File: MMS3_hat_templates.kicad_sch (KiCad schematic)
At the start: 10 parts

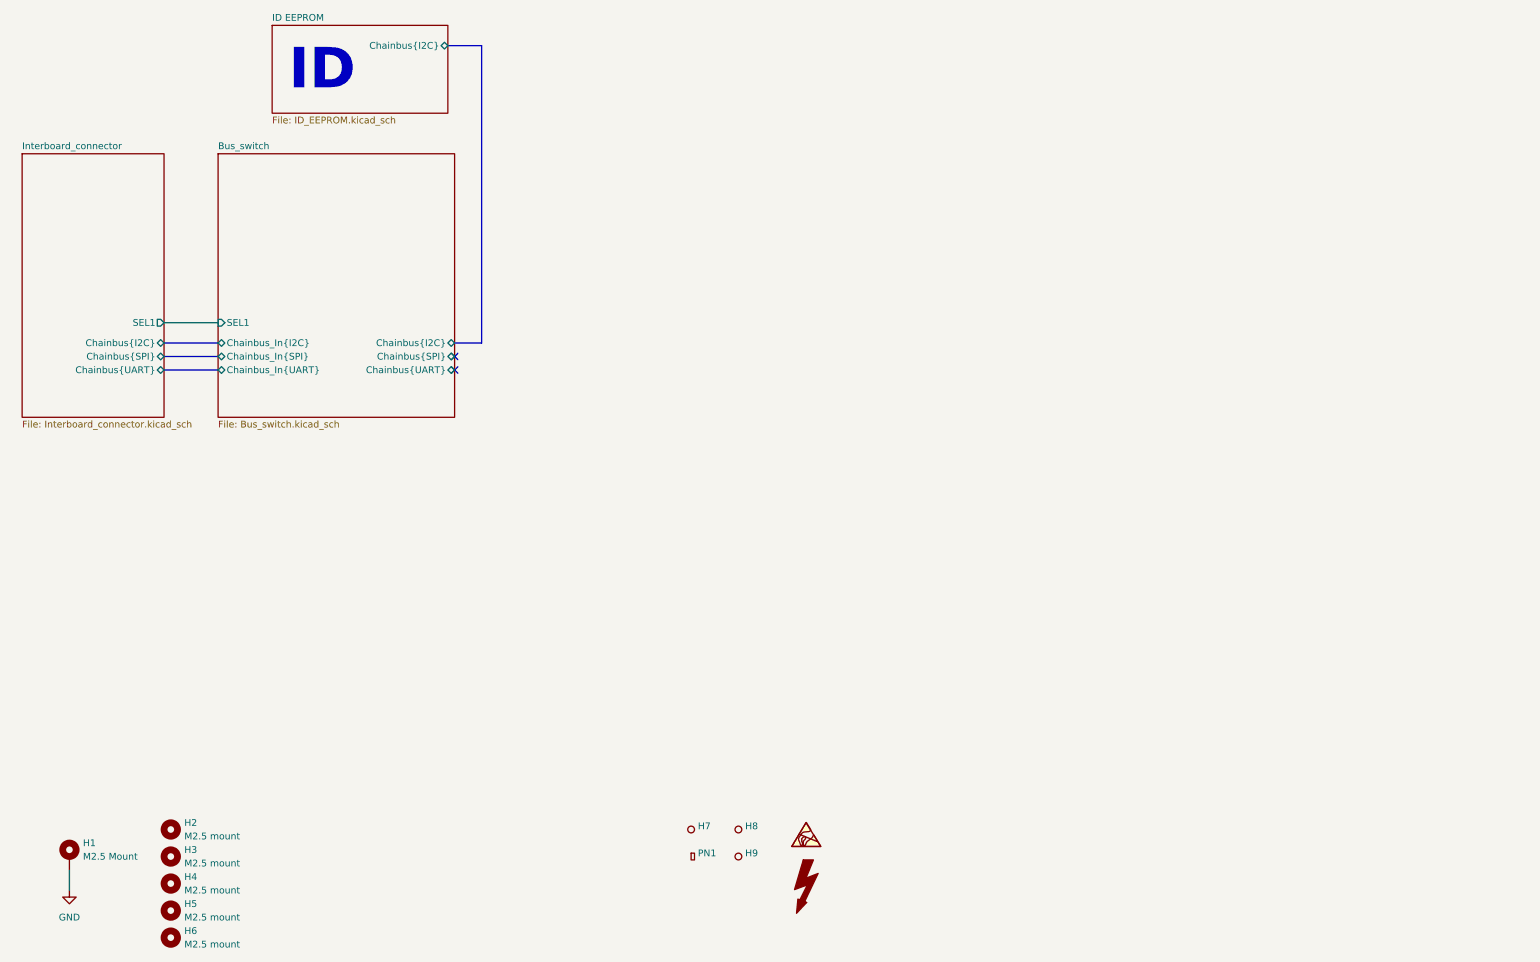
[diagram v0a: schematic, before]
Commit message: first steps
 thermocouple and GPIO expander sheets done
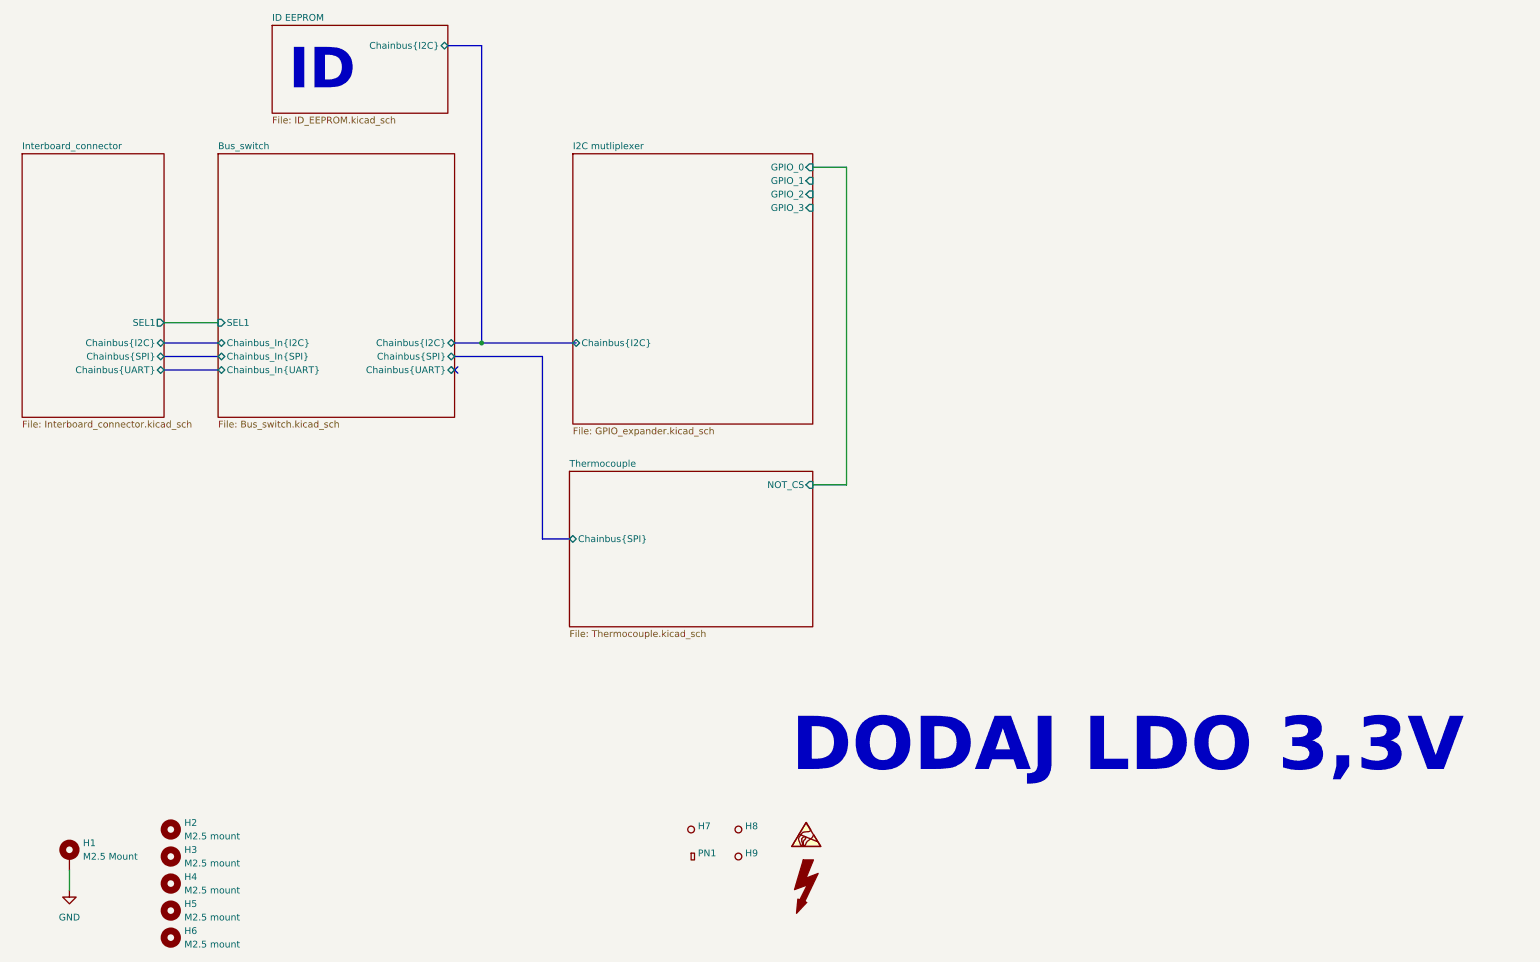
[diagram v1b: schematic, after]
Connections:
- no-connect marks 2 -> 1
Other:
- added sheet I2C mutliplexer (GPIO_expander.kicad_sch)
- added sheet Thermocouple (Thermocouple.kicad_sch)
- note added: "DODAJ LDO 3,3V"
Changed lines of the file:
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@@
 		)
 	)
-	(no_connect
-		(at 96.52 82.55)
+	(text "DODAJ LDO 3,3V "
+		(exclude_from_sim no)
+		(at 223.012 153.162 0)
+		(effects
+			(font
+				(size 10 10)
+				(thickness 4.4)
+				(bold yes)
+			)
+		)
+	)
+	(junction
+		(at 101.6 77.47)
+		(diameter 0)
+		(color 0 0 0 0)
 	)
 	(no_connect
-		(at 96.52 80.01)
+		(at 96.52 82.55)
 	)
 	(bus
@@
 		)
 	)
+	(bus
+		(pts
+			(xy 101.6 77.47) (xy 119.38 77.47)
+		)
+		(stroke
+			(width 0)
+			(type default)
+		)
+	)
 	(wire
 		(pts
@@
 		)
 	)
+	(wire
+		(pts
+			(xy 170.18 104.14) (xy 170.18 44.45)
+		)
+		(stroke
+			(width 0)
+			(type default)
+		)
+	)
 	(bus
 		(pts
@@
 		)
 	)
+	(bus
+		(pts
+			(xy 96.52 80.01) (xy 113.03 80.01)
+		)
+		(stroke
+			(width 0)
+			(type default)
+		)
+	)
+	(bus
+		(pts
+			(xy 113.03 80.01) (xy 113.03 114.3)
+		)
+		(stroke
+			(width 0)
+			(type default)
+		)
+	)
+	(wire
+		(pts
+			(xy 170.18 44.45) (xy 163.83 44.45)
+		)
+		(stroke
+			(width 0)
+			(type default)
+		)
+	)
+	(bus
+		(pts
+			(xy 113.03 114.3) (xy 118.11 114.3)
+		)
+		(stroke
+			(width 0)
+			(type default)
+		)
+	)
+	(wire
+		(pts
+			(xy 163.83 104.14) (xy 170.18 104.14)
+		)
+		(stroke
+			(width 0)
+			(type default)
+		)
+	)
 	(image
 		(at 74.93 59.69)
@@
 				)
 			)
+		)
+	)
+	(sheet
+		(at 118.745 41.91)
+		(size 45.085 50.8)
+		(exclude_from_sim no)
+		(in_bom yes)
+		(on_board yes)
+		(dnp no)
+		(fields_autoplaced yes)
+		(stroke
+			(width 0.1524)
+			(type solid)
+		)
+		(fill
+			(color 0 0 0 0.0000)
+		)
+		(property "Sheetname" "I2C mutliplexer"
+			(at 118.745 41.1984 0)
+			(effects
+				(font
+					(size 1.27 1.27)
+				)
+				(justify left bottom)
+			)
+		)
+		(property "Sheetfile" "GPIO_expander.kicad_sch"
+			(at 118.745 93.2946 0)
+			(effects
+				(font
+					(size 1.27 1.27)
+				)
+				(justify left top)
+			)
+		)
+		(pin "Chainbus{I2C}" bidirectional
+			(at 118.745 77.47 180)
+			(effects
+				(font
+					(size 1.27 1.27)
+				)
+				(justify left)
+			)
+		)
+		(pin "GPIO_0" input
+			(at 163.83 44.45 0)
+			(effects
+				(font
+					(size 1.27 1.27)
+				)
+				(justify right)
+			)
+		)
+		(pin "GPIO_1" input
+			(at 163.83 46.99 0)
+			(effects
+				(font
+					(size 1.27 1.27)
+				)
+				(justify right)
+			)
+		)
+		(pin "GPIO_2" input
+			(at 163.83 49.53 0)
+			(effects
+				(font
+					(size 1.27 1.27)
+				)
+				(justify right)
+			)
+		)
+		(pin "GPIO_3" input
+			(at 163.83 52.07 0)
+			(effects
+				(font
+					(size 1.27 1.27)
+				)
+				(justify right)
+			)
+		)
+		(instances
+			(project "MMS3_hat_templates"
+				(path "/6596548a-44e0-46d8-8624-fd71cf4a3e17"
+					(page "5")
+				)
+			)
+		)
+	)
+	(sheet
+		(at 118.11 101.6)
+		(size 45.72 29.21)
+		(exclude_from_sim no)
+		(in_bom yes)
+		(on_board yes)
+		(dnp no)
+		(fields_autoplaced yes)
+		(stroke
+			(width 0.1524)
+			(type solid)
+		)
+		(fill
+			(color 0 0 0 0.0000)
+		)
+		(property "Sheetname" "Thermocouple"
+			(at 118.11 100.8884 0)
+			(effects
+				(font
+					(size 1.27 1.27)
+				)
+				(justify left bottom)
+			)
+		)
+		(property "Sheetfile" "Thermocouple.kicad_sch"
+			(at 118.11 131.3946 0)
+			(effects
+				(font
+					(size 1.27 1.27)
+				)
+				(justify left top)
+			)
+		)
+		(pin "Chainbus{SPI}" bidirectional
+			(at 118.11 114.3 180)
+			(effects
+				(font
+					(size 1.27 1.27)
+				)
+				(justify left)
+			)
+		)
+		(pin "NOT_CS" input
+			(at 163.83 104.14 0)
+			(effects
+				(font
+					(size 1.27 1.27)
+				)
+				(justify right)
+			)
+		)
+		(instances
+			(project "MMS3_hat_templates"
+				(path "/6596548a-44e0-46d8-8624-fd71cf4a3e17"
+					(page "6")
+				)
+			)

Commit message: done ( v 1.0 - check required )
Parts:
- removed H7, H8, H9: ~, PCM_JLCPCB:Hole_Tooling_JLCPCB, symbol PCM_JLCPCB-Manufacturing:Tooling Hole, PCM_JLCPCB, 1.152mm
- added C13, C14, C15: 10u, Capacitor_SMD:CP_Elec_3x5.4, symbol Device:C_Polarized
- added U14: AZ1117H-3.3TRE1, Package_TO_SOT_SMD:SOT-223-3_TabPin2, symbol Regulator_Linear:AZ1117H-ADJ
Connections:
- net GND: now also C13.2, C14.2, C15.2, U14.1 (GND)
- new net +3V3: C14.1, C15.1, U14.2 (VO)
- new net +5V: C13.1, U14.3 (VI)
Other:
- added sheet Thermocouple1 (Thermocouple.kicad_sch)
- added sheet Thermocouple2 (Thermocouple.kicad_sch)
- added sheet Thermocouple3 (Thermocouple.kicad_sch)
- added sheet Thermocouple4 (Thermocouple.kicad_sch)
- added sheet Thermocouple5 (Thermocouple.kicad_sch)
- added sheet Thermocouple6 (Thermocouple.kicad_sch)
- added sheet Thermocouple7 (Thermocouple.kicad_sch)
- added sheet Thermocouple8 (Thermocouple.kicad_sch)
- sheet I2C mutliplexer ports: added GPIO_4, GPIO_5, GPIO_6, GPIO_7, GPIO_8; removed none
- note removed: "DODAJ LDO 3,3V"

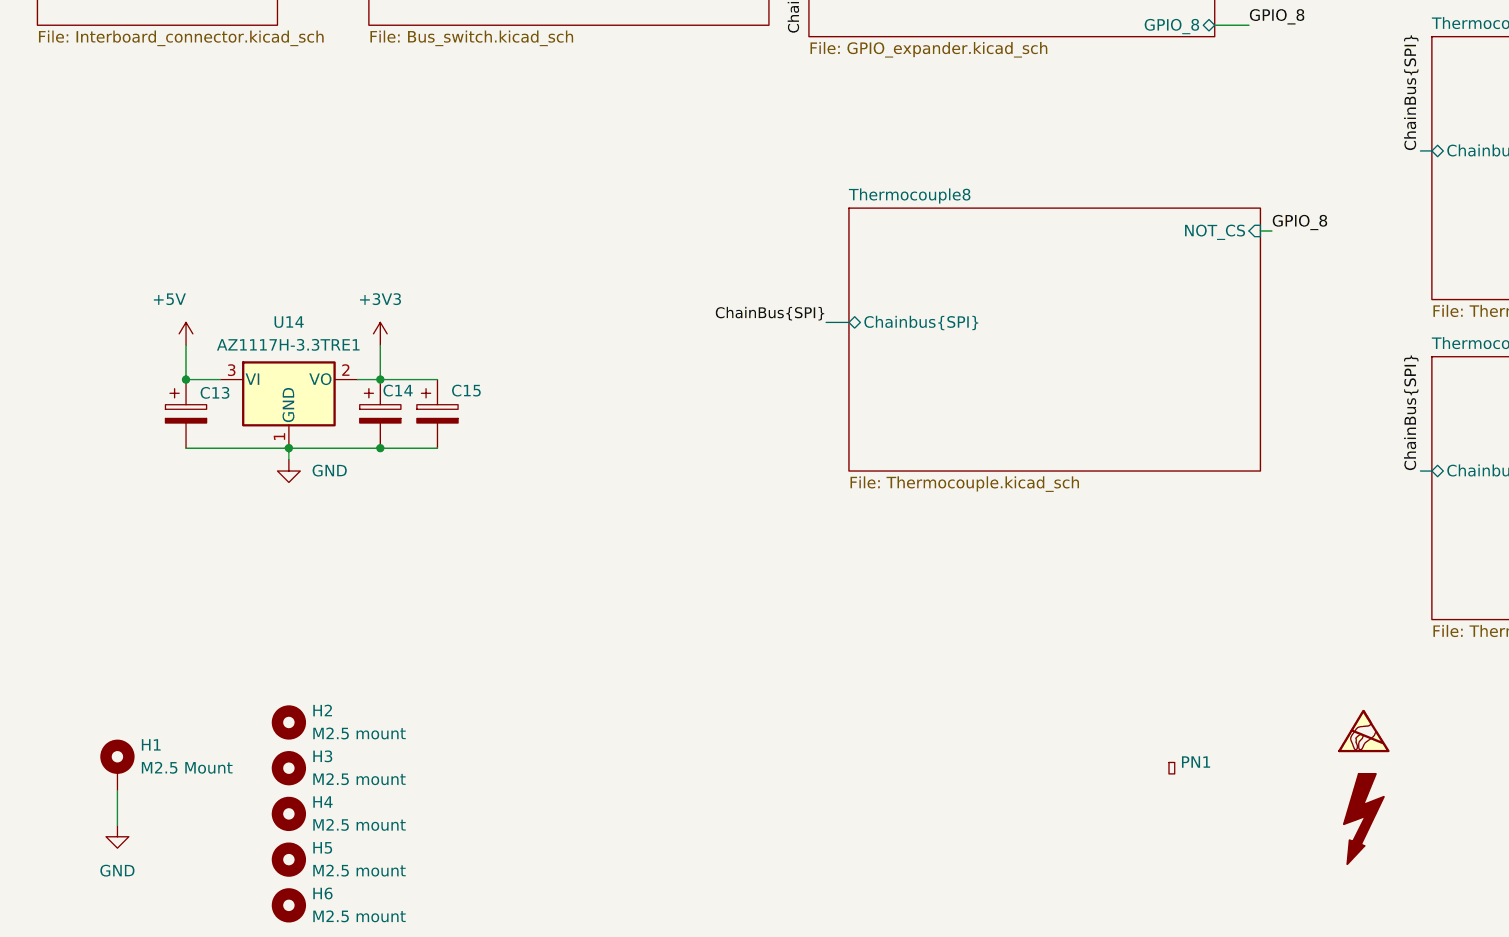
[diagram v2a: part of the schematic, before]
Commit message: fixed selected led polarity
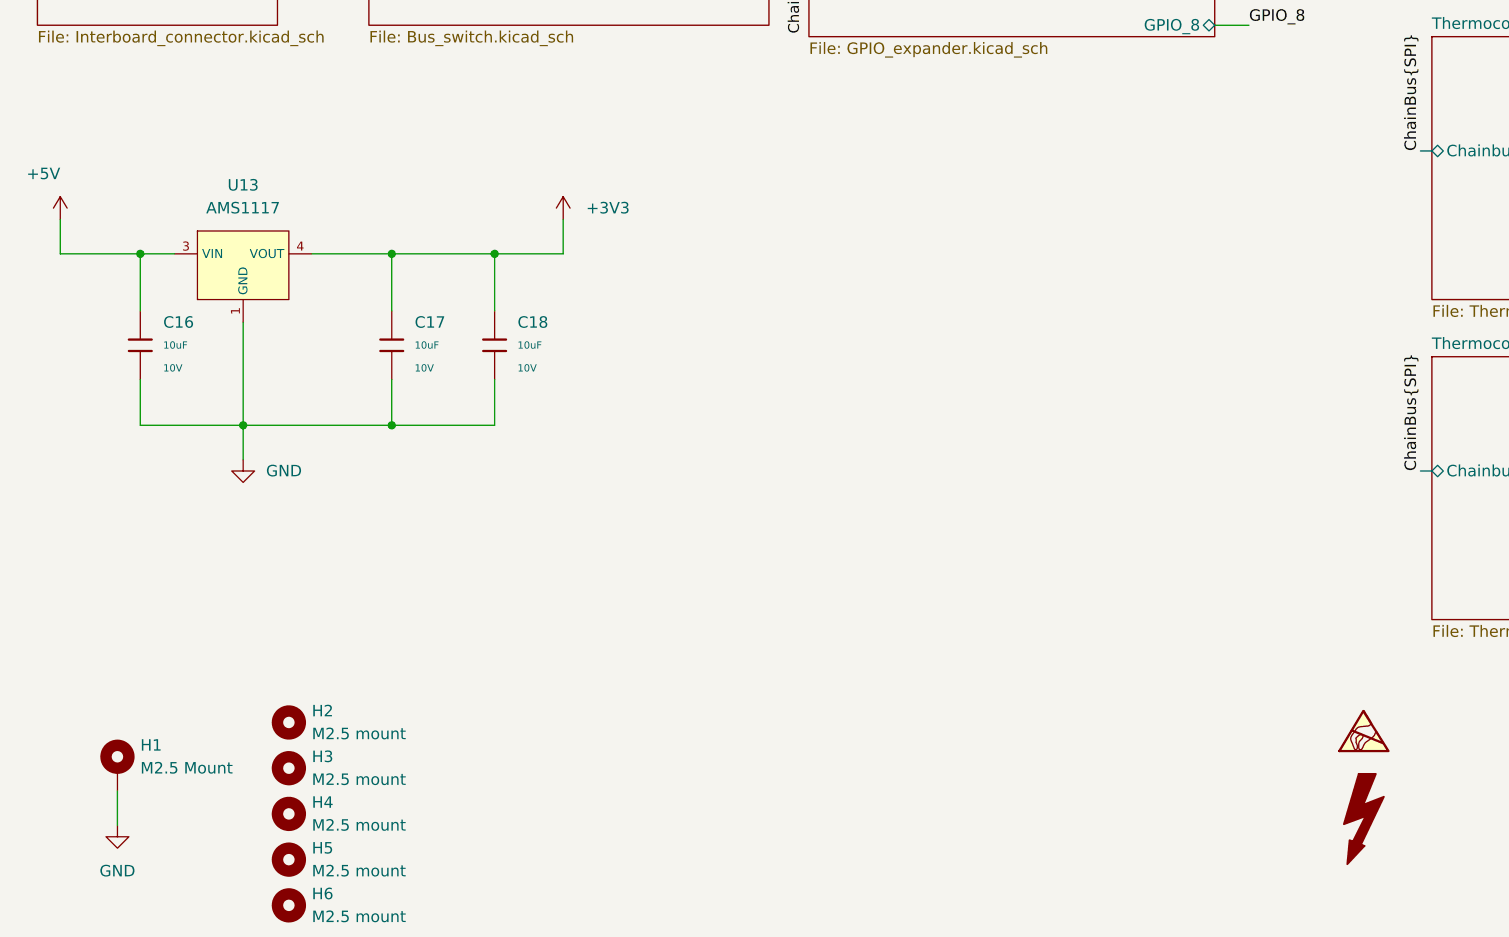
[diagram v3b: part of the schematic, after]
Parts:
- removed C13, C14, C15: 10u, Capacitor_SMD:CP_Elec_3x5.4, symbol Device:C_Polarized
- removed PN1: ~, PCM_JLCPCB:Part_Num_JLCPCB, symbol PCM_JLCPCB-Manufacturing:Part Number, PCM_JLCPCB, 0.8x0.15mm
- removed U14: AZ1117H-3.3TRE1, Package_TO_SOT_SMD:SOT-223-3_TabPin2, symbol Regulator_Linear:AZ1117H-ADJ
- added C16, C17, C18: 10uF, PCM_JLCPCB:C_0603, symbol PCM_JLCPCB-Capacitors:0603,10uF
- added U13: AMS1117, PCM_JLCPCB:SOT-223-3_L6.5-W3.4-P2.30-LS7.0-BR, symbol PCM_JLCPCB-Power:LDO, 3.3V, 1A
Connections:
- net +3V3: now also C17.1, C18.1, U13.2 (VOUT), U13.4 (VOUT)
- net +5V: now also C16.1, U13.3 (VIN)
- net GND: now also C16.2, C17.2, C18.2, U13.1 (GND)
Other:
- removed sheet Thermocouple8
